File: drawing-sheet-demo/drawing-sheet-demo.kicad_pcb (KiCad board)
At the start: 2 copper layers, 17.9 x 24.5 mm, 8 parts, among them J1 Conn_01x02_Pin, U1 LMC555xM

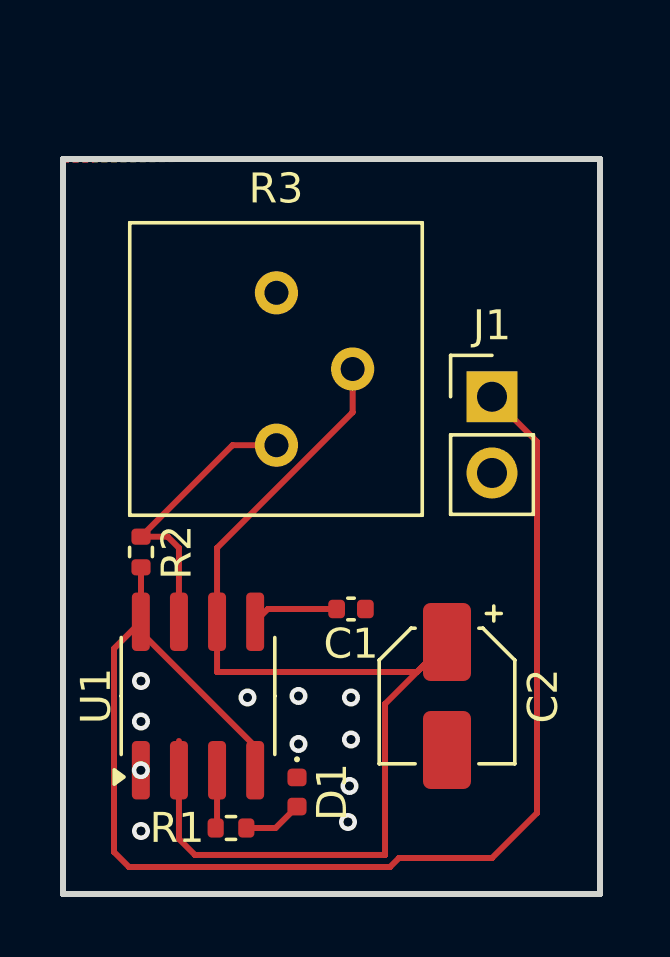
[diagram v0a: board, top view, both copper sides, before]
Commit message: better match the Rocket Engine part review process
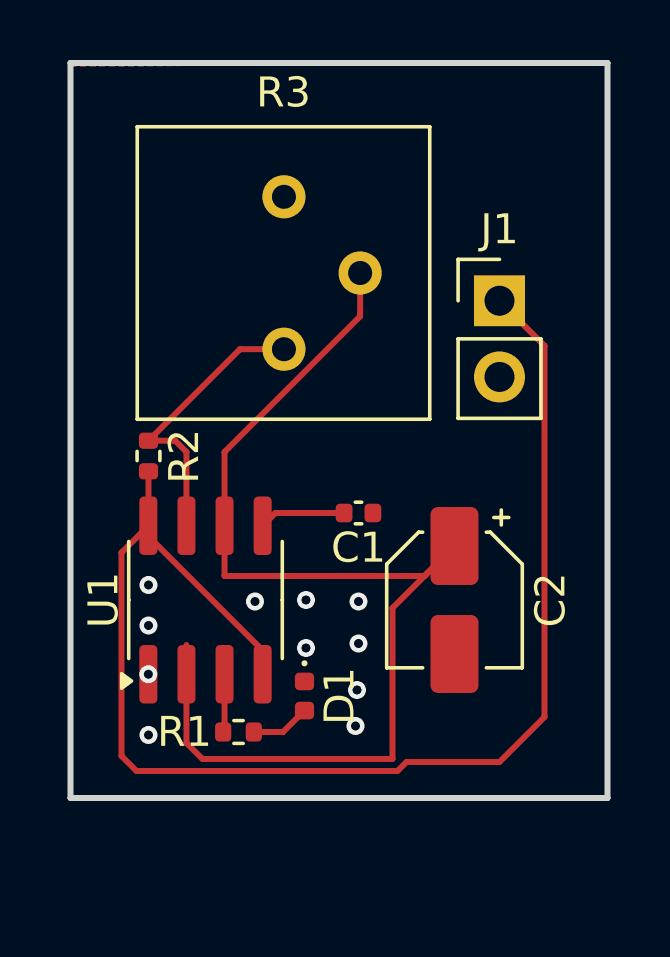
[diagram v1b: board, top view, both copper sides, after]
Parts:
- moved R1 3.21 mm to (119.8, 125.6)
- moved C1 3.21 mm to (123.8, 118.3)
- moved C2 3.21 mm to (127.0, 121.2)
- moved J1 3.21 mm to (128.6, 111.2)
- moved R3 3.21 mm to (121.4, 112.8)
- moved U1 3.21 mm to (118.8, 121.2)
- moved D1 3.21 mm to (122.0, 124.4)
- moved R2 3.21 mm to (116.8, 116.4)
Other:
- board text added: "2025-05-23 2025-05-23 2025-05-23 2025-05-23 2025-05-23"
- board text added: "LB MC ER SD AK"
- board text added: "Lucas Bennett Maya Chen Elijah Rivers Sofia Delgado Aiden Kapoor"
- board text removed: "05/22/2025"
- board text removed: "CJW"
- board text removed: "JS MS"
- board text removed: "Joe Schmoe"
- board text removed: "Mary Sue"
